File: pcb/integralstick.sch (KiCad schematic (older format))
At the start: 9 parts, among them J2 CONN_INTEGRALSTICK_MCU_DEVICE

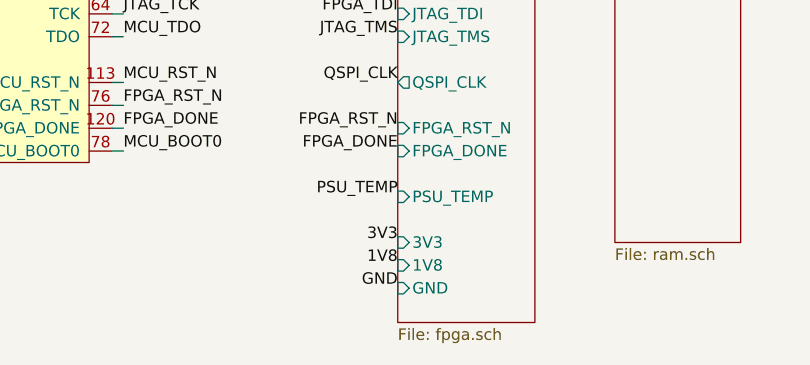
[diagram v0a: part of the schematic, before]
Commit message: Added missing 1V8 clock. Tweaked planes. Added some layer change caps.
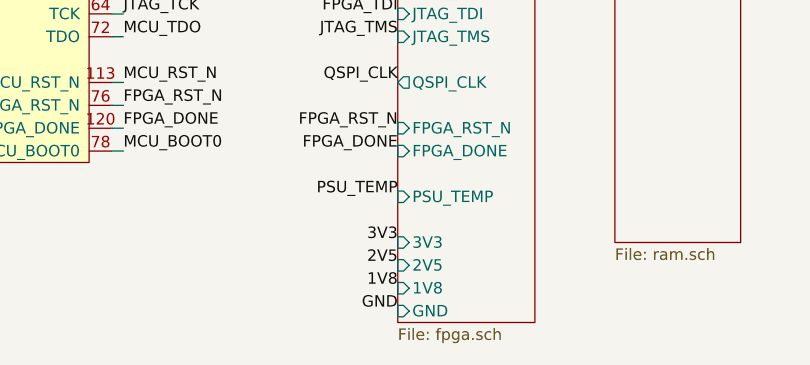
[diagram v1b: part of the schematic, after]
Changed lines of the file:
@@
 F9 "PSU_TEMP" I L 2700 5050 50
 F10 "3V3" I L 2700 5250 50
-F11 "GND" I L 2700 5450 50
-F12 "1V8" I L 2700 5350 50
+F11 "GND" I L 2700 5550 50
+F12 "1V8" I L 2700 5450 50
+F13 "2V5" I L 2700 5350 50
 $EndSheet
 $Sheet
@@
 Text Label 2700 5250 2    50   ~ 0
 3V3
-Text Label 2700 5450 2    50   ~ 0
+Text Label 2700 5550 2    50   ~ 0
 GND
 Text Label 1500 4850 0    50   ~ 0
@@
 Text Label 10050 2500 2    50   ~ 0
 3V3
+Text Label 2700 5450 2    50   ~ 0
+1V8
 Text Label 2700 5350 2    50   ~ 0
-1V8
+2V5
 $EndSCHEMATC

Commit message: Continued work on layout. Added some layer crossing caps. Initial power plane placement.
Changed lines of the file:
@@
 Sheet 1 8
 Title "INTEGRALSTICK Compute Module"
-Date "2018-11-14"
+Date "2018-11-19"
 Rev "0.1"
 Comp "Andrew D. Zonenberg"
@@
 $EndSheet
 $Sheet
-S 2700 4000 600  1600
+S 2700 4000 600  1700
 U 5B6B702C
 F0 "FPGA" 50
@@
 F9 "PSU_TEMP" I L 2700 5050 50
 F10 "3V3" I L 2700 5250 50
-F11 "GND" I L 2700 5550 50
+F11 "GND" I L 2700 5650 50
 F12 "1V8" I L 2700 5450 50
 F13 "2V5" I L 2700 5350 50
+F14 "1V0" I L 2700 5550 50
 $EndSheet
 $Sheet
@@
 Text Label 2700 5250 2    50   ~ 0
 3V3
-Text Label 2700 5550 2    50   ~ 0
+Text Label 2700 5650 2    50   ~ 0
 GND
 Text Label 1500 4850 0    50   ~ 0
@@
 Text Label 2700 5350 2    50   ~ 0
 2V5
+Text Label 2700 5550 2    50   ~ 0
+1V0
 $EndSCHEMATC

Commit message: Added lots of test points
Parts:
- added TP12, TP13, TP14, TP15, TP16, TP17, TP18, TP19: TESTPAD, azonenberg_pcb:TESTPOINT_BARETRACE_328UM, symbol conn:CONN_01X01
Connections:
- net GND: now also TP12.1 (P1), TP13.1 (P1), TP14.1 (P1), TP15.1 (P1), TP16.1 (P1), TP17.1 (P1), TP18.1 (P1), TP19.1 (P1)
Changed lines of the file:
@@
 Sheet 1 8
 Title "INTEGRALSTICK Compute Module"
-Date "2018-11-23"
+Date "2018-11-29"
 Rev "0.1"
 Comp "Andrew D. Zonenberg"
@@
 Text Label 2700 5550 2    50   ~ 0
 1V0
+$Comp
+L conn:CONN_01X01 TP12
+U 1 1 5C00F507
+P 10250 2800
+F 0 "TP12" H 10328 2841 50  0000 L CNN
+F 1 "TESTPAD" H 10328 2750 50  0000 L CNN
+F 2 "azonenberg_pcb:TESTPOINT_BARETRACE_328UM" H 10250 2800 50  0001 C CNN
+F 3 "" H 10250 2800 50  0001 C CNN
+	1    10250 2800
+	1    0    0    -1
+$EndComp
+Text Label 10050 2800 2    50   ~ 0
+GND
+$Comp
+L conn:CONN_01X01 TP13
+U 1 1 5C011C4C
+P 10250 3100
+F 0 "TP13" H 10328 3141 50  0000 L CNN
+F 1 "TESTPAD" H 10328 3050 50  0000 L CNN
+F 2 "azonenberg_pcb:TESTPOINT_BARETRACE_328UM" H 10250 3100 50  0001 C CNN
+F 3 "" H 10250 3100 50  0001 C CNN
+	1    10250 3100
+	1    0    0    -1
+$EndComp
+Text Label 10050 3100 2    50   ~ 0
+GND
+$Comp
+L conn:CONN_01X01 TP14
+U 1 1 5C017C13
+P 10250 3350
+F 0 "TP14" H 10328 3391 50  0000 L CNN
+F 1 "TESTPAD" H 10328 3300 50  0000 L CNN
+F 2 "azonenberg_pcb:TESTPOINT_BARETRACE_328UM" H 10250 3350 50  0001 C CNN
+F 3 "" H 10250 3350 50  0001 C CNN
+	1    10250 3350
+	1    0    0    -1
+$EndComp
+Text Label 10050 3350 2    50   ~ 0
+GND
+$Comp
+L conn:CONN_01X01 TP15
+U 1 1 5C01BAEF
+P 10250 3600
+F 0 "TP15" H 10328 3641 50  0000 L CNN
+F 1 "TESTPAD" H 10328 3550 50  0000 L CNN
+F 2 "azonenberg_pcb:TESTPOINT_BARETRACE_328UM" H 10250 3600 50  0001 C CNN
+F 3 "" H 10250 3600 50  0001 C CNN
+	1    10250 3600
+	1    0    0    -1
+$EndComp
+Text Label 10050 3600 2    50   ~ 0
+GND
+$Comp
+L conn:CONN_01X01 TP16
+U 1 1 5C01FB32
+P 10250 3850
+F 0 "TP16" H 10328 3891 50  0000 L CNN
+F 1 "TESTPAD" H 10328 3800 50  0000 L CNN
+F 2 "azonenberg_pcb:TESTPOINT_BARETRACE_328UM" H 10250 3850 50  0001 C CNN
+F 3 "" H 10250 3850 50  0001 C CNN
+	1    10250 3850
+	1    0    0    -1
+$EndComp
+Text Label 10050 3850 2    50   ~ 0
+GND
+$Comp
+L conn:CONN_01X01 TP17
+U 1 1 5C027F8E
+P 10250 4100
+F 0 "TP17" H 10328 4141 50  0000 L CNN
+F 1 "TESTPAD" H 10328 4050 50  0000 L CNN
+F 2 "azonenberg_pcb:TESTPOINT_BARETRACE_328UM" H 10250 4100 50  0001 C CNN
+F 3 "" H 10250 4100 50  0001 C CNN
+	1    10250 4100
+	1    0    0    -1
+$EndComp
+Text Label 10050 4100 2    50   ~ 0
+GND
+$Comp
+L conn:CONN_01X01 TP18
+U 1 1 5C03F491
+P 10250 4350
+F 0 "TP18" H 10328 4391 50  0000 L CNN
+F 1 "TESTPAD" H 10328 4300 50  0000 L CNN
+F 2 "azonenberg_pcb:TESTPOINT_BARETRACE_328UM" H 10250 4350 50  0001 C CNN
+F 3 "" H 10250 4350 50  0001 C CNN
+	1    10250 4350
+	1    0    0    -1
+$EndComp
+Text Label 10050 4350 2    50   ~ 0
+GND
+$Comp
+L conn:CONN_01X01 TP19
+U 1 1 5C04B243
+P 10250 4600
+F 0 "TP19" H 10328 4641 50  0000 L CNN
+F 1 "TESTPAD" H 10328 4550 50  0000 L CNN
+F 2 "azonenberg_pcb:TESTPOINT_BARETRACE_328UM" H 10250 4600 50  0001 C CNN
+F 3 "" H 10250 4600 50  0001 C CNN
+	1    10250 4600
+	1    0    0    -1
+$EndComp
+Text Label 10050 4600 2    50   ~ 0
+GND
 $EndSCHEMATC

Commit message: Updated integralstick schematic to fix library paths. No content changes.
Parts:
- TP10, TP12, TP13, TP14, TP15, TP16, TP17, TP18, TP19, TP4, TP5, TP6, TP7, TP8, TP9: symbol conn:CONN_01X01 -> integralstick-rescue:CONN_01X01-conn
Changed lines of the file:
@@
 $EndComp
 $Comp
-L conn:CONN_01X01 TP4
+L integralstick-rescue:CONN_01X01-conn TP4
 U 1 1 5D3FC56A
 P 10250 1050
@@
 GND
 $Comp
-L conn:CONN_01X01 TP5
+L integralstick-rescue:CONN_01X01-conn TP5
 U 1 1 5D3FCCF4
 P 10250 1250
@@
 GND
 $Comp
-L conn:CONN_01X01 TP6
+L integralstick-rescue:CONN_01X01-conn TP6
 U 1 1 5D3FE87E
 P 10250 1500
@@
 1V0
 $Comp
-L conn:CONN_01X01 TP7
+L integralstick-rescue:CONN_01X01-conn TP7
 U 1 1 5D3FEB71
 P 10250 1750
@@
 1V2
 $Comp
-L conn:CONN_01X01 TP8
+L integralstick-rescue:CONN_01X01-conn TP8
 U 1 1 5D4007A9
 P 10250 2000
@@
 1V8
 $Comp
-L conn:CONN_01X01 TP9
+L integralstick-rescue:CONN_01X01-conn TP9
 U 1 1 5D402358
 P 10250 2250
@@
 2V5
 $Comp
-L conn:CONN_01X01 TP10
+L integralstick-rescue:CONN_01X01-conn TP10
 U 1 1 5D403FC0
 P 10250 2500
@@
 1V0
 $Comp
-L conn:CONN_01X01 TP12
+L integralstick-rescue:CONN_01X01-conn TP12
 U 1 1 5C00F507
 P 10250 2800
@@
 GND
 $Comp
-L conn:CONN_01X01 TP13
+L integralstick-rescue:CONN_01X01-conn TP13
 U 1 1 5C011C4C
 P 10250 3100
@@
 GND
 $Comp
-L conn:CONN_01X01 TP14
+L integralstick-rescue:CONN_01X01-conn TP14
 U 1 1 5C017C13
 P 10250 3350
@@
 GND
 $Comp
-L conn:CONN_01X01 TP15
+L integralstick-rescue:CONN_01X01-conn TP15
 U 1 1 5C01BAEF
 P 10250 3600
@@
 GND
 $Comp
-L conn:CONN_01X01 TP16
+L integralstick-rescue:CONN_01X01-conn TP16
 U 1 1 5C01FB32
 P 10250 3850
@@
 GND
 $Comp
-L conn:CONN_01X01 TP17
+L integralstick-rescue:CONN_01X01-conn TP17
 U 1 1 5C027F8E
 P 10250 4100
@@
 GND
 $Comp
-L conn:CONN_01X01 TP18
+L integralstick-rescue:CONN_01X01-conn TP18
 U 1 1 5C03F491
 P 10250 4350
@@
 GND
 $Comp
-L conn:CONN_01X01 TP19
+L integralstick-rescue:CONN_01X01-conn TP19
 U 1 1 5C04B243
 P 10250 4600
